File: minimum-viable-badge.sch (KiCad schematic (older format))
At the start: 33 parts, among them J101 EDGE_CONNECTOR, P101 USB, P102 BATTERY, P103 POT_LONG, P104 BUTTON_A, P105 BUTTON_B, P106 POT_SHORT, P107 MECH, P108 MECH, P109 MECH, Q101 S8050, Q102 S8050, SW101 PRGM, SW102 RESET, U101 ESP32-WROOM, U102 CP2102

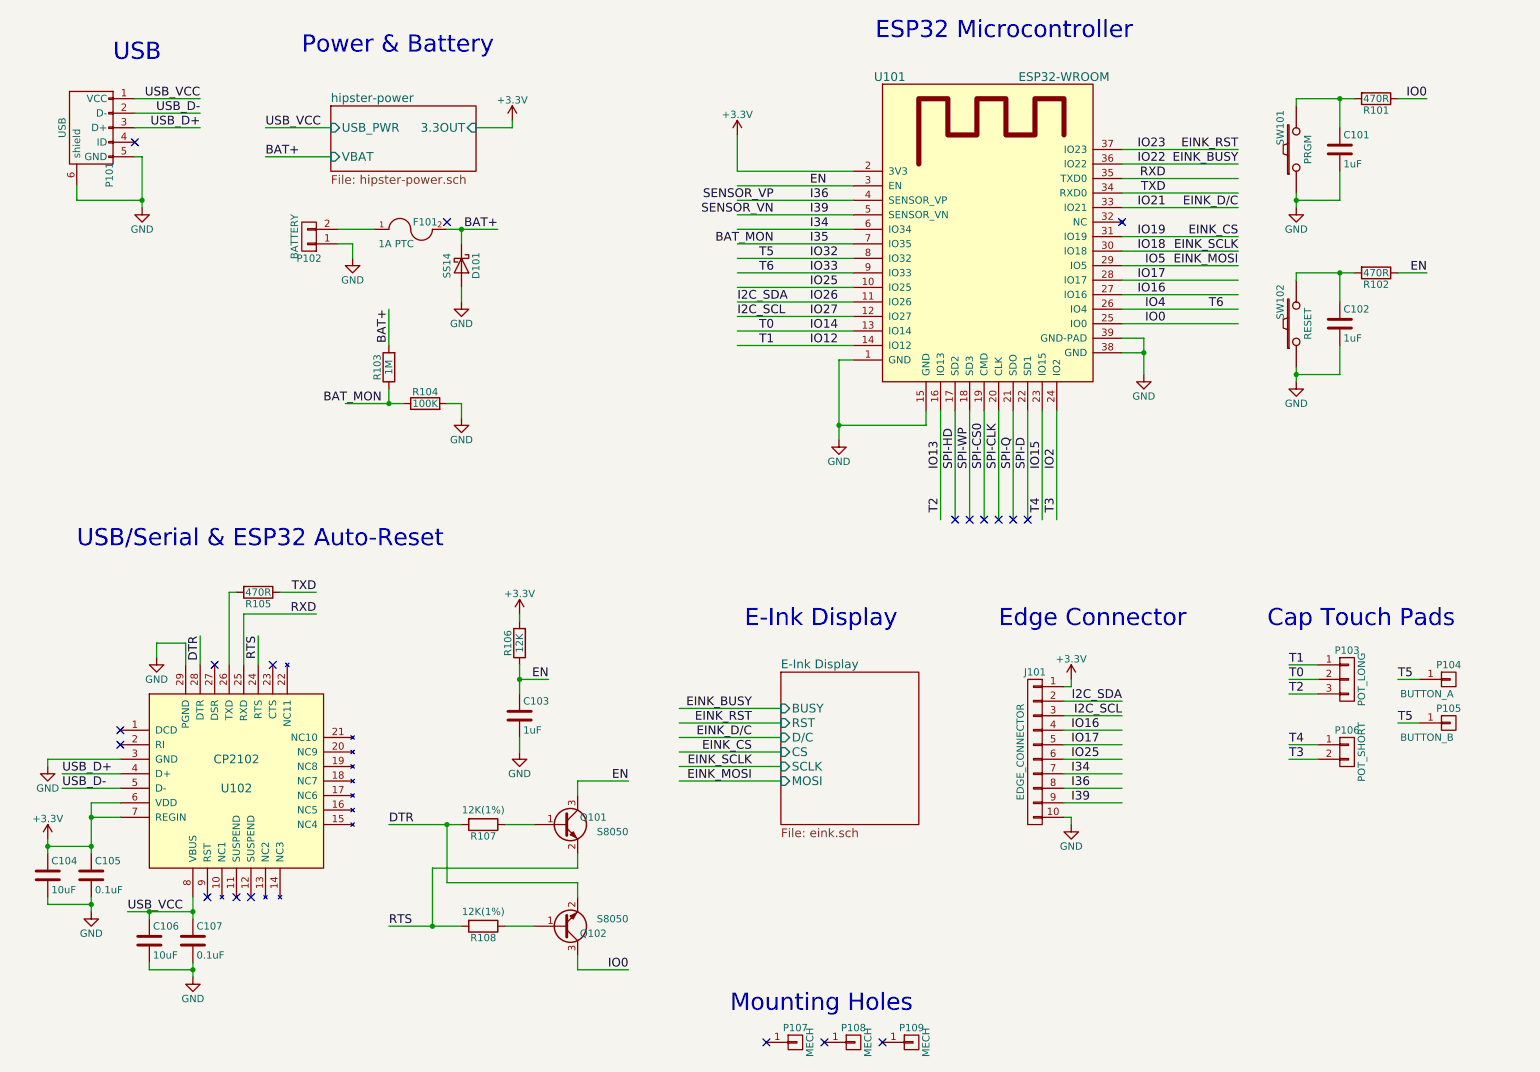
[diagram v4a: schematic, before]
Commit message: Set component footprints.
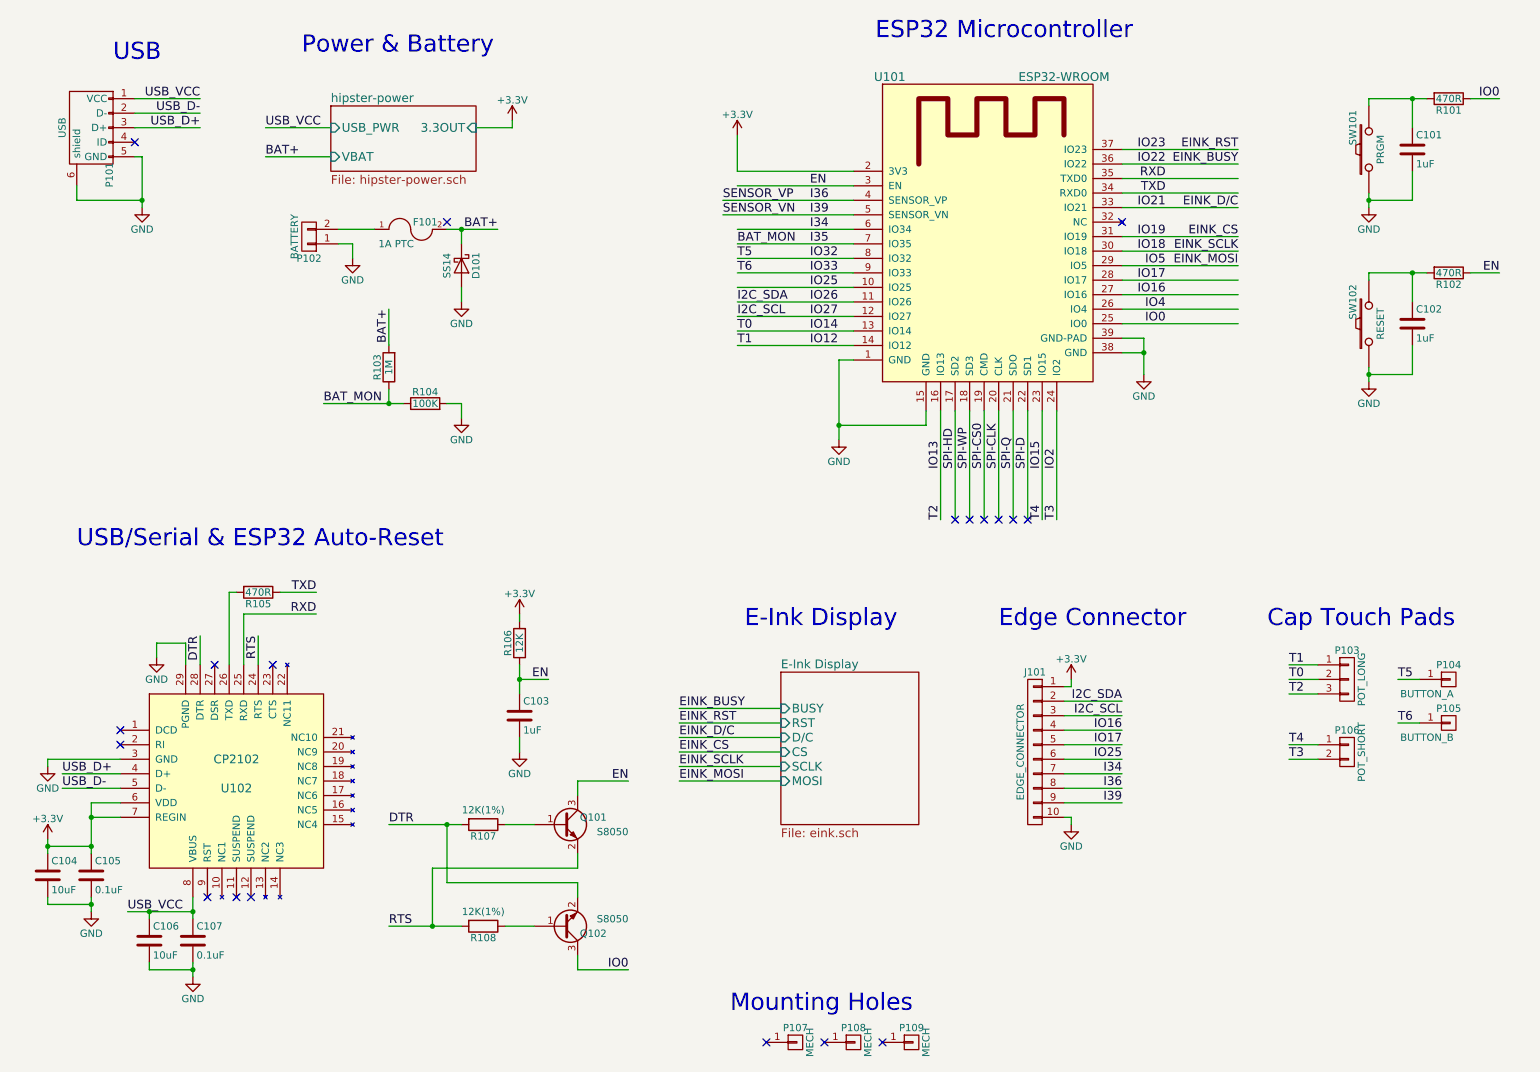
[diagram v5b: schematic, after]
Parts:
- J101: footprint (none) -> Pin_Headers:Pin_Header_Angled_1x10_Pitch2.54mm
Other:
- moved on the sheet: C101, C102, R101, R102, SW101, SW102
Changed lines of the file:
@@
 Text Label 6100 2050 0    60   ~ 0
 I34
-Text Label 5850 1950 2    60   ~ 0
+Text Label 5500 1950 0    60   ~ 0
 SENSOR_VN
-Text Label 5850 1850 2    60   ~ 0
+Text Label 5500 1850 0    60   ~ 0
 SENSOR_VP
 $Comp
@@
 L R R101
 U 1 1 59270A5B
-P 10000 1150
-F 0 "R101" V 10080 1150 50  0000 C CNN
-F 1 "470R" V 10000 1150 50  0000 C CNN
-F 2 "Resistors_SMD:R_0603_HandSoldering" V 9930 1150 50  0001 C CNN
-F 3 "" H 10000 1150 50  0000 C CNN
-F 4 "311-470HRCT-ND" V 10100 1150 60  0001 C CNN "Digikey PN"
-F 5 "http://www.digikey.com.au/product-detail/en/yageo/RC0603FR-07470RL/311-470HRCT-ND/730203" V 10100 1150 60  0001 C CNN "Link"
-F 6 "RC0603FR-07470RL" V 10100 1150 60  0001 C CNN "Manufacturer PN"
-F 7 "0.10" V 10100 1150 60  0001 C CNN "Unit Cost"
-	1    10000 1150
+P 10500 1150
+F 0 "R101" V 10580 1150 50  0000 C CNN
+F 1 "470R" V 10500 1150 50  0000 C CNN
+F 2 "Resistors_SMD:R_0603_HandSoldering" V 10430 1150 50  0001 C CNN
+F 3 "" H 10500 1150 50  0000 C CNN
+F 4 "311-470HRCT-ND" V 10600 1150 60  0001 C CNN "Digikey PN"
+F 5 "http://www.digikey.com.au/product-detail/en/yageo/RC0603FR-07470RL/311-470HRCT-ND/730203" V 10600 1150 60  0001 C CNN "Link"
+F 6 "RC0603FR-07470RL" V 10600 1150 60  0001 C CNN "Manufacturer PN"
+F 7 "0.10" V 10600 1150 60  0001 C CNN "Unit Cost"
+	1    10500 1150
 	0    1    1    0
 $EndComp
@@
 L C C101
 U 1 1 59270B98
-P 9750 1500
-F 0 "C101" H 9775 1600 50  0000 L CNN
-F 1 "1uF" H 9775 1400 50  0000 L CNN
-F 2 "Capacitors_SMD:C_0603_HandSoldering" H 9788 1350 50  0001 C CNN
-F 3 "" H 9750 1500 50  0000 C CNN
-	1    9750 1500
+P 10250 1500
+F 0 "C101" H 10275 1600 50  0000 L CNN
+F 1 "1uF" H 10275 1400 50  0000 L CNN
+F 2 "Capacitors_SMD:C_0603_HandSoldering" H 10288 1350 50  0001 C CNN
+F 3 "" H 10250 1500 50  0000 C CNN
+	1    10250 1500
 	1    0    0    -1
 $EndComp
@@
 L SW_PUSH SW101
 U 1 1 59270D01
-P 9450 1500
-F 0 "SW101" H 9600 1610 50  0000 C CNN
-F 1 "PRGM" H 9450 1420 50  0000 C CNN
-F 2 "Buttons_Switches_ThroughHole:SW_PUSH_SMALL" H 9450 1500 50  0001 C CNN
-F 3 "" H 9450 1500 50  0000 C CNN
-	1    9450 1500
+P 9950 1500
+F 0 "SW101" H 10100 1610 50  0000 C CNN
+F 1 "PRGM" H 9950 1420 50  0000 C CNN
+F 2 "Buttons_Switches_ThroughHole:SW_PUSH_SMALL" H 9950 1500 50  0001 C CNN
+F 3 "" H 9950 1500 50  0000 C CNN
+	1    9950 1500
 	0    -1   -1   0
 $EndComp
@@
 L GND #PWR04
 U 1 1 59270E7E
-P 9450 1900
-F 0 "#PWR04" H 9450 1650 50  0001 C CNN
-F 1 "GND" H 9450 1750 50  0000 C CNN
-F 2 "" H 9450 1900 50  0000 C CNN
-F 3 "" H 9450 1900 50  0000 C CNN
-	1    9450 1900
-	1    0    0    -1
-$EndComp
-Text Label 10350 1150 2    60   ~ 0
+P 9950 1900
+F 0 "#PWR04" H 9950 1650 50  0001 C CNN
+F 1 "GND" H 9950 1750 50  0000 C CNN
+F 2 "" H 9950 1900 50  0000 C CNN
+F 3 "" H 9950 1900 50  0000 C CNN
+	1    9950 1900
+	1    0    0    -1
+$EndComp
+Text Label 10850 1150 2    60   ~ 0
 IO0
 $Comp
 L R R102
 U 1 1 59271D5C
-P 10000 2350
-F 0 "R102" V 10080 2350 50  0000 C CNN
-F 1 "470R" V 10000 2350 50  0000 C CNN
-F 2 "Resistors_SMD:R_0603_HandSoldering" V 9930 2350 50  0001 C CNN
-F 3 "" H 10000 2350 50  0000 C CNN
-F 4 "311-470HRCT-ND" V 10100 1150 60  0001 C CNN "Digikey PN"
-F 5 "http://www.digikey.com.au/product-detail/en/yageo/RC0603FR-07470RL/311-470HRCT-ND/730203" V 10100 1150 60  0001 C CNN "Link"
-F 6 "RC0603FR-07470RL" V 10100 1150 60  0001 C CNN "Manufacturer PN"
-F 7 "0.10" V 10100 1150 60  0001 C CNN "Unit Cost"
-	1    10000 2350
+P 10500 2350
+F 0 "R102" V 10580 2350 50  0000 C CNN
+F 1 "470R" V 10500 2350 50  0000 C CNN
+F 2 "Resistors_SMD:R_0603_HandSoldering" V 10430 2350 50  0001 C CNN
+F 3 "" H 10500 2350 50  0000 C CNN
+F 4 "311-470HRCT-ND" V 10600 1150 60  0001 C CNN "Digikey PN"
+F 5 "http://www.digikey.com.au/product-detail/en/yageo/RC0603FR-07470RL/311-470HRCT-ND/730203" V 10600 1150 60  0001 C CNN "Link"
+F 6 "RC0603FR-07470RL" V 10600 1150 60  0001 C CNN "Manufacturer PN"
+F 7 "0.10" V 10600 1150 60  0001 C CNN "Unit Cost"
+	1    10500 2350
 	0    1    1    0
 $EndComp
@@
 L C C102
 U 1 1 59271D62
-P 9750 2700
-F 0 "C102" H 9775 2800 50  0000 L CNN
-F 1 "1uF" H 9775 2600 50  0000 L CNN
-F 2 "Capacitors_SMD:C_0603_HandSoldering" H 9788 2550 50  0001 C CNN
-F 3 "" H 9750 2700 50  0000 C CNN
-	1    9750 2700
+P 10250 2700
+F 0 "C102" H 10275 2800 50  0000 L CNN
+F 1 "1uF" H 10275 2600 50  0000 L CNN
+F 2 "Capacitors_SMD:C_0603_HandSoldering" H 10288 2550 50  0001 C CNN
+F 3 "" H 10250 2700 50  0000 C CNN
+	1    10250 2700
 	1    0    0    -1
 $EndComp
@@
 L SW_PUSH SW102
 U 1 1 59271D68
-P 9450 2700
-F 0 "SW102" H 9600 2810 50  0000 C CNN
-F 1 "RESET" H 9450 2620 50  0000 C CNN
-F 2 "Buttons_Switches_ThroughHole:SW_PUSH_SMALL" H 9450 2700 50  0001 C CNN
-F 3 "" H 9450 2700 50  0000 C CNN
-	1    9450 2700
+P 9950 2700
+F 0 "SW102" H 10100 2810 50  0000 C CNN
+F 1 "RESET" H 9950 2620 50  0000 C CNN
+F 2 "Buttons_Switches_ThroughHole:SW_PUSH_SMALL" H 9950 2700 50  0001 C CNN
+F 3 "" H 9950 2700 50  0000 C CNN
+	1    9950 2700
 	0    -1   -1   0
 $EndComp
@@
 L GND #PWR05
 U 1 1 59271D6E
-P 9450 3100
-F 0 "#PWR05" H 9450 2850 50  0001 C CNN
-F 1 "GND" H 9450 2950 50  0000 C CNN
-F 2 "" H 9450 3100 50  0000 C CNN
-F 3 "" H 9450 3100 50  0000 C CNN
-	1    9450 3100
-	1    0    0    -1
-$EndComp
-Text Label 10350 2350 2    60   ~ 0
+P 9950 3100
+F 0 "#PWR05" H 9950 2850 50  0001 C CNN
+F 1 "GND" H 9950 2950 50  0000 C CNN
+F 2 "" H 9950 3100 50  0000 C CNN
+F 3 "" H 9950 3100 50  0000 C CNN
+	1    9950 3100
+	1    0    0    -1
+$EndComp
+Text Label 10850 2350 2    60   ~ 0
 EN
 $Comp
@@
 Text Label 2350 1350 0    60   ~ 0
 USB_VCC
-Text Label 8950 2600 2    60   ~ 0
-T6
-Text Label 7800 4000 1    60   ~ 0
+Text Label 7800 4050 1    60   ~ 0
 T3
-Text Label 7700 4000 1    60   ~ 0
+Text Label 7700 4050 1    60   ~ 0
 T4
-Text Label 5750 2750 0    60   ~ 0
+Text Label 5600 2750 0    60   ~ 0
 T0
-Text Label 7000 4000 1    60   ~ 0
+Text Label 7000 4050 1    60   ~ 0
 T2
 Text Label 5600 2650 0    60   ~ 0
@@
 Text Label 5600 2550 0    60   ~ 0
 I2C_SDA
-Text Label 5850 2150 2    60   ~ 0
+Text Label 5600 2150 0    60   ~ 0
 BAT_MON
 Text Label 9400 5250 0    60   ~ 0
@@
 Text Label 9400 5700 0    60   ~ 0
 T3
-Text Label 3150 3250 2    60   ~ 0
+Text Label 2750 3250 0    60   ~ 0
 BAT_MON
-Text Label 5750 2850 0    60   ~ 0
+Text Label 5600 2850 0    60   ~ 0
 T1
 Text Label 9400 5150 0    60   ~ 0
@@
 	5600 2050 6400 2050
 Wire Wire Line
-	5600 1950 6400 1950
-Wire Wire Line
-	5600 1850 6400 1850
+	5500 1950 6400 1950
+Wire Wire Line
+	5500 1850 6400 1850
 Wire Wire Line
 	5600 1750 6400 1750
@@
 	8250 1500 9050 1500
 Wire Wire Line
-	9450 1800 9450 1900
-Wire Wire Line
-	9450 1850 9750 1850
-Wire Wire Line
-	9750 1850 9750 1650
-Connection ~ 9450 1850
-Wire Wire Line
-	9750 1350 9750 1150
-Wire Wire Line
-	9450 1150 9850 1150
-Wire Wire Line
-	9450 1200 9450 1150
-Connection ~ 9750 1150
-Wire Wire Line
-	10150 1150 10350 1150
-Wire Wire Line
-	9450 3000 9450 3100
-Wire Wire Line
-	9450 3050 9750 3050
-Wire Wire Line
-	9750 3050 9750 2850
-Connection ~ 9450 3050
-Wire Wire Line
-	9750 2550 9750 2350
-Wire Wire Line
-	9450 2350 9850 2350
-Wire Wire Line
-	9450 2400 9450 2350
-Connection ~ 9750 2350
-Wire Wire Line
-	10150 2350 10350 2350
+	9950 1800 9950 1900
+Wire Wire Line
+	9950 1850 10250 1850
+Wire Wire Line
+	10250 1850 10250 1650
+Connection ~ 9950 1850
+Wire Wire Line
+	10250 1350 10250 1150
+Wire Wire Line
+	9950 1150 10350 1150
+Wire Wire Line
+	9950 1200 9950 1150
+Connection ~ 10250 1150
+Wire Wire Line
+	10650 1150 10850 1150
+Wire Wire Line
+	9950 3000 9950 3100
+Wire Wire Line
+	9950 3050 10250 3050
+Wire Wire Line
+	10250 3050 10250 2850
+Connection ~ 9950 3050
+Wire Wire Line
+	10250 2550 10250 2350
+Wire Wire Line
+	9950 2350 10350 2350
+Wire Wire Line
+	9950 2400 9950 2350
+Connection ~ 10250 2350
+Wire Wire Line
+	10650 2350 10850 2350
 Wire Wire Line
 	4100 4750 4100 4700
@@
 	3200 3150 3200 3250
 Wire Wire Line
-	2900 3250 3300 3250
+	2750 3250 3300 3250
 Wire Wire Line
 	3600 3250 3700 3250
@@
 T5
 Text Label 10150 5450 0    60   ~ 0
+T6
+Text Label 5600 2250 0    60   ~ 0
 T5
-Text Label 5750 2250 0    60   ~ 0
-T5
-Text Label 5750 2350 0    60   ~ 0
+Text Label 5600 2350 0    60   ~ 0
 T6
 Wire Wire Line
@@
 F 0 "J101" H 7650 6200 50  0000 C CNN
 F 1 "EDGE_CONNECTOR" V 7750 5650 50  0000 C CNN
-F 2 "" H 7650 5650 50  0001 C CNN
+F 2 "Pin_Headers:Pin_Header_Angled_1x10_Pitch2.54mm" H 7650 5650 50  0001 C CNN
 F 3 "" H 7650 5650 50  0001 C CNN
 	1    7650 5650
@@
 Wire Wire Line
 	5900 5850 5200 5850
-Text Label 5700 5850 2    60   ~ 0
+Text Label 5200 5850 0    60   ~ 0
 EINK_MOSI
-Text Label 5700 5750 2    60   ~ 0
+Text Label 5200 5750 0    60   ~ 0
 EINK_SCLK
-Text Label 5700 5650 2    60   ~ 0
+Text Label 5200 5650 0    60   ~ 0
 EINK_CS
-Text Label 5700 5550 2    60   ~ 0
+Text Label 5200 5550 0    60   ~ 0
 EINK_D/C
-Text Label 5700 5450 2    60   ~ 0
+Text Label 5200 5450 0    60   ~ 0
 EINK_RST
-Text Label 5700 5350 2    60   ~ 0
+Text Label 5200 5350 0    60   ~ 0
 EINK_BUSY
 Text Notes 2600 850  0    118  ~ 0
@@
 Text Label 6100 1950 0    60   ~ 0
 I39
-Text Label 7900 5500 0    60   ~ 0
+Text Label 8250 5500 2    60   ~ 0
 IO16
-Text Label 7900 5600 0    60   ~ 0
+Text Label 8250 5600 2    60   ~ 0
 IO17
-Text Label 7900 5800 0    60   ~ 0
+Text Label 8250 5800 2    60   ~ 0
 I34
 NoConn ~ 7100 4050
@@
 NoConn ~ 7500 4050
 NoConn ~ 7600 4050
-Text Label 7900 5900 0    60   ~ 0
+Text Label 8250 5900 2    60   ~ 0
 I36
-Text Label 7900 5700 0    60   ~ 0
+Text Label 8250 5700 2    60   ~ 0
 IO25
-Text Label 7900 6000 0    60   ~ 0
+Text Label 8250 6000 2    60   ~ 0
 I39
 Wire Wire Line

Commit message: Updated to use new switch.
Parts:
- SW101, SW102: footprint Buttons_Switches_ThroughHole:SW_PUSH_SMALL -> libs:K2-1107st
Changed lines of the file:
@@
 F 0 "SW101" H 10100 1610 50  0000 C CNN
 F 1 "PRGM" H 9950 1420 50  0000 C CNN
-F 2 "Buttons_Switches_ThroughHole:SW_PUSH_SMALL" H 9950 1500 50  0001 C CNN
+F 2 "libs:K2-1107st" H 9950 1500 50  0001 C CNN
 F 3 "" H 9950 1500 50  0000 C CNN
 	1    9950 1500
@@
 F 0 "SW102" H 10100 2810 50  0000 C CNN
 F 1 "RESET" H 9950 2620 50  0000 C CNN
-F 2 "Buttons_Switches_ThroughHole:SW_PUSH_SMALL" H 9950 2700 50  0001 C CNN
+F 2 "libs:K2-1107st" H 9950 2700 50  0001 C CNN
 F 3 "" H 9950 2700 50  0000 C CNN
 	1    9950 2700
